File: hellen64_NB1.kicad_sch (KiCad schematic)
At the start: 170 parts, among them J1 USB_B_Mini, J11 Conn_01x01, J12 Conn_01x01, J13 Conn_01x01, J14 Conn_01x01, J15 Conn_01x01, J16 Conn_01x01, J17 Conn_01x01, J18 Conn_01x01, J19 Conn_01x01, J2 Conn_01x05_Male, J20 Conn_01x01, J21 Conn_01x01, J22 Conn_01x01, J24 Conn_01x01, J25 AudioJack3_SwitchTR, J27 Conn_01x06, J3 Conn_01x06, J4 Conn_02x12_Odd_Even, J5 USB_B, M1 Module-input-0.1, M10 Module-power12-0.2, M11 Module-power5-0.2, M12 Module-wbo-0.2, M13 Module-can-0.1, M2 Module-ign8-0.1, M3 Module-mcu-0.3, M4 Module-sd-0.1, M5 Module-output-0.2, M6 Module-dinput4-0.1, M7 Module-stlink-0.1, M8 Module-can-0.1, M9 Module-knock-0.1, P1 Pad, P10 Pad, P11 Pad, P12 Pad, P13 Pad, P14 Pad, P15 Pad, P17 Pad, P18 Pad, P19 Pad, P2 176122-6_2nd, P20 Pad, P22 Pad, P23 Pad, P24 Pad, P25 Pad, P26 Pad, P27 Pad, P28 Pad, P29 Pad, P3 Pad, P30 Pad, P31 Pad, P32 Pad, P34 Pad, P38 Pad, P4 Pad, P40 Pad, P43 Pad, P44 Pad, P46 Pad, P47 Pad, P48 Pad, P49 Pad, P5 Pad, P50 Pad, P51 Pad, P52 Pad, P53 Pad, P55 Pad, P56 Pad, P6 Pad, P7 Pad, P8 Pad, P9 Pad, U1 LIS2DW12TR, U2 MPX4_MAP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

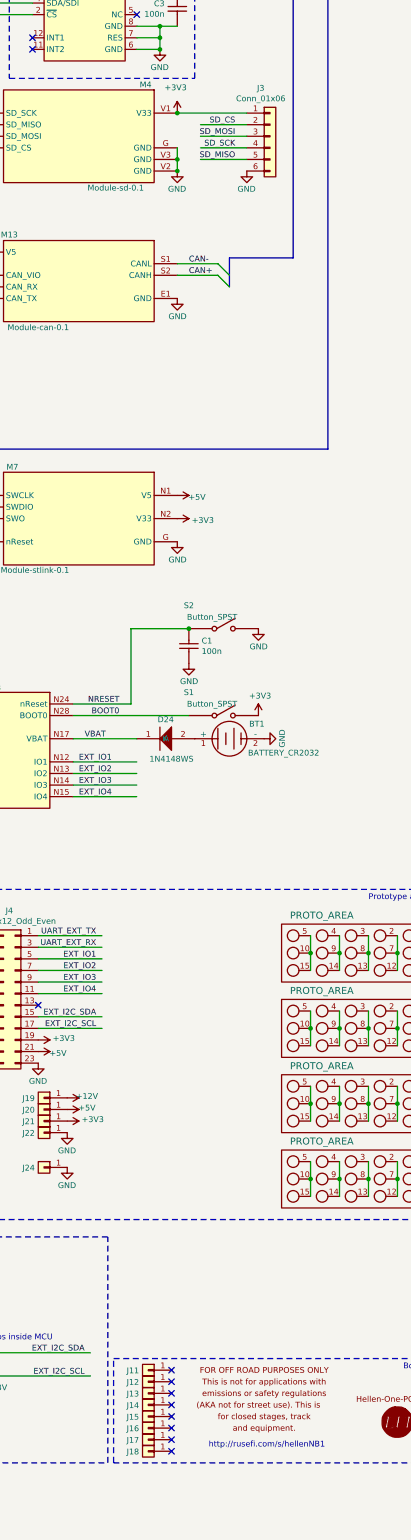
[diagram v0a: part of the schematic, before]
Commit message: new pcb board shape, dims & holes for NB1 + trying to fit components inside (remove SD-card ext.header)
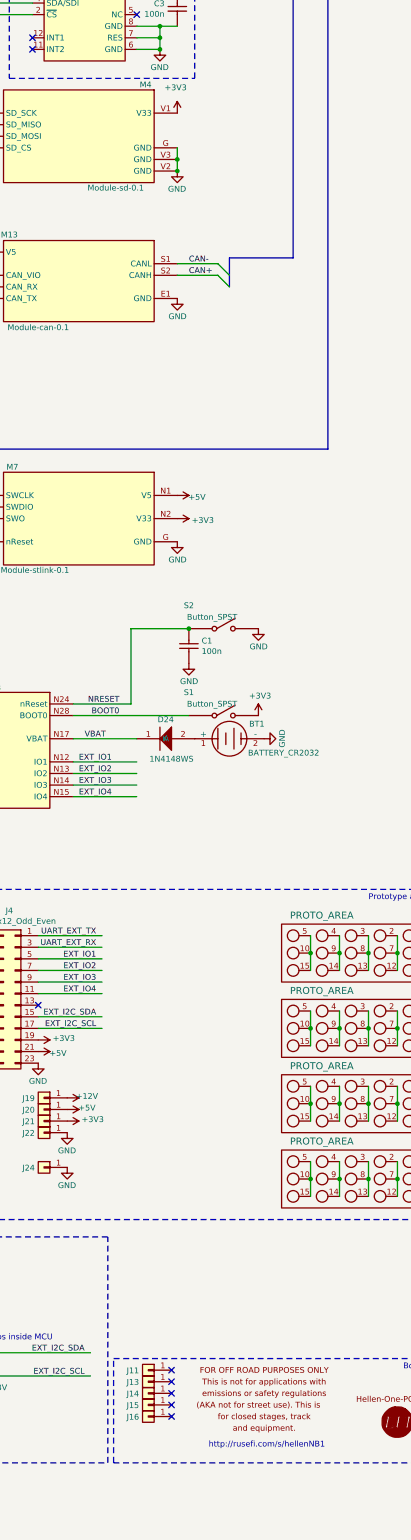
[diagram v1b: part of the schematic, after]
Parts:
- removed J12, J17, J18: Conn_01x01, MountingHole:MountingHole_4.5mm_Pad, symbol Connector_Generic:Conn_01x01
- removed J3: Conn_01x06, Connector_PinHeader_2.54mm:PinHeader_1x06_P2.54mm_Vertical, symbol Connector_Generic:Conn_01x06
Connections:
- no-connect marks 63 -> 60
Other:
- moved on the sheet: J13, J14, J15, J16
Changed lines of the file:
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@@
   (junction (at 515.62 74.93) (diameter 1.016) (color 0 0 0 0))
   (junction (at 515.62 77.47) (diameter 1.016) (color 0 0 0 0))
-  (junction (at 519.43 91.44) (diameter 1.016) (color 0 0 0 0))
   (junction (at 519.43 101.6) (diameter 1.016) (color 0 0 0 0))
   (junction (at 519.43 104.14) (diameter 1.016) (color 0 0 0 0))
@@
   (no_connect (at 518.16 374.65))
   (no_connect (at 518.16 377.19))
-  (no_connect (at 518.16 379.73))
-  (no_connect (at 518.16 382.27))
-  (no_connect (at 518.16 384.81))
   (bus_entry (at 77.47 27.94) (size 2.54 2.54)
     (stroke (width 0.1524) (type solid) (color 0 0 0 0))
@@
     (stroke (width 0) (type solid) (color 0 0 0 0))
   )
-  (wire (pts (xy 519.43 91.44) (xy 534.67 91.44))
-    (stroke (width 0) (type solid) (color 0 0 0 0))
-  )
   (wire (pts (xy 519.43 99.06) (xy 519.43 101.6))
     (stroke (width 0) (type solid) (color 0 0 0 0))
@@
     (stroke (width 0) (type solid) (color 0 0 0 0))
   )
-  (wire (pts (xy 524.51 93.98) (xy 534.67 93.98))
-    (stroke (width 0) (type solid) (color 0 0 0 0))
-  )
-  (wire (pts (xy 524.51 96.52) (xy 534.67 96.52))
-    (stroke (width 0) (type solid) (color 0 0 0 0))
-  )
-  (wire (pts (xy 524.51 99.06) (xy 534.67 99.06))
-    (stroke (width 0) (type solid) (color 0 0 0 0))
-  )
-  (wire (pts (xy 524.51 101.6) (xy 534.67 101.6))
-    (stroke (width 0) (type solid) (color 0 0 0 0))
-  )
   (wire (pts (xy 548.64 271.78) (xy 548.64 275.59))
     (stroke (width 0) (type solid) (color 0 0 0 0))
@@
     (effects (font (size 1.27 1.27)) (justify left bottom))
   )
-  (label "SD_CS" (at 532.13 93.98 180)
-    (effects (font (size 1.27 1.27)) (justify right bottom))
-  )
-  (label "SD_MOSI" (at 532.13 96.52 180)
-    (effects (font (size 1.27 1.27)) (justify right bottom))
-  )
-  (label "SD_SCK" (at 532.13 99.06 180)
-    (effects (font (size 1.27 1.27)) (justify right bottom))
-  )
-  (label "SD_MISO" (at 532.13 101.6 180)
-    (effects (font (size 1.27 1.27)) (justify right bottom))
-  )
   (symbol (lib_id "power:+5V") (at 31.75 318.77 90) (unit 1)
     (in_bom yes) (on_board yes)
@@
     (pin "1")
   )
-  (symbol (lib_id "power:GND") (at 534.67 104.14 0) (mirror y) (unit 1)
-    (in_bom yes) (on_board yes)
-    (property "Reference" "#PWR0103" (id 0) (at 534.67 110.49 0)
-      (effects (font (size 1.27 1.27)) hide)
-    )
-    (property "Value" "GND" (id 1) (at 534.6192 108.0834 0))
-    (property "Footprint" "" (id 2) (at 534.67 104.14 0)
-      (effects (font (size 1.27 1.27)) hide)
-    )
-    (property "Datasheet" "" (id 3) (at 534.67 104.14 0)
-      (effects (font (size 1.27 1.27)) hide)
-    )
-    (pin "1")
-  )
   (symbol (lib_id "power:GND") (at 537.21 204.47 0) (unit 1)
     (in_bom yes) (on_board yes)
@@
   (symbol (lib_id "Connector_Generic:Conn_01x01") (at 513.08 369.57 0) (mirror y) (unit 1)
     (in_bom yes) (on_board yes)
-    (property "Reference" "J12" (id 0) (at 511.048 369.6716 0)
+    (property "Reference" "J13" (id 0) (at 511.048 369.6716 0)
       (effects (font (size 1.27 1.27)) (justify left))
     )
@@
   (symbol (lib_id "Connector_Generic:Conn_01x01") (at 513.08 372.11 0) (mirror y) (unit 1)
     (in_bom yes) (on_board yes)
-    (property "Reference" "J13" (id 0) (at 511.048 372.2116 0)
+    (property "Reference" "J14" (id 0) (at 511.048 372.2116 0)
       (effects (font (size 1.27 1.27)) (justify left))
     )
@@
   (symbol (lib_id "Connector_Generic:Conn_01x01") (at 513.08 374.65 0) (mirror y) (unit 1)
     (in_bom yes) (on_board yes)
-    (property "Reference" "J14" (id 0) (at 511.048 374.7516 0)
+    (property "Reference" "J15" (id 0) (at 511.048 374.7516 0)
       (effects (font (size 1.27 1.27)) (justify left))
     )
@@
   (symbol (lib_id "Connector_Generic:Conn_01x01") (at 513.08 377.19 0) (mirror y) (unit 1)
     (in_bom yes) (on_board yes)
-    (property "Reference" "J15" (id 0) (at 511.048 377.2916 0)
+    (property "Reference" "J16" (id 0) (at 511.048 377.2916 0)
       (effects (font (size 1.27 1.27)) (justify left))
     )
@@
     (pin "1")
   )
-  (symbol (lib_id "Connector_Generic:Conn_01x01") (at 513.08 379.73 0) (mirror y) (unit 1)
-    (in_bom yes) (on_board yes)
-    (property "Reference" "J16" (id 0) (at 511.048 379.8316 0)
-      (effects (font (size 1.27 1.27)) (justify left))
-    )
-    (property "Value" "Conn_01x01" (id 1) (at 511.048 380.9746 0)
-      (effects (font (size 1.27 1.27)) (justify left) hide)
-    )
-    (property "Footprint" "MountingHole:MountingHole_4.5mm_Pad" (id 2) (at 513.08 379.73 0)
-      (effects (font (size 1.27 1.27)) hide)
-    )
-    (property "Datasheet" "~" (id 3) (at 513.08 379.73 0)
-      (effects (font (size 1.27 1.27)) hide)
-    )
-    (pin "1")
-  )
-  (symbol (lib_id "Connector_Generic:Conn_01x01") (at 513.08 382.27 0) (mirror y) (unit 1)
-    (in_bom yes) (on_board yes)
-    (property "Reference" "J17" (id 0) (at 511.048 382.3716 0)
-      (effects (font (size 1.27 1.27)) (justify left))
-    )
-    (property "Value" "Conn_01x01" (id 1) (at 511.048 383.5146 0)
-      (effects (font (size 1.27 1.27)) (justify left) hide)
-    )
-    (property "Footprint" "MountingHole:MountingHole_4.5mm_Pad" (id 2) (at 513.08 382.27 0)
-      (effects (font (size 1.27 1.27)) hide)
-    )
-    (property "Datasheet" "~" (id 3) (at 513.08 382.27 0)
-      (effects (font (size 1.27 1.27)) hide)
-    )
-    (pin "1")
-  )
-  (symbol (lib_id "Connector_Generic:Conn_01x01") (at 513.08 384.81 0) (mirror y) (unit 1)
-    (in_bom yes) (on_board yes)
-    (property "Reference" "J18" (id 0) (at 511.048 384.9116 0)
-      (effects (font (size 1.27 1.27)) (justify left))
-    )
-    (property "Value" "Conn_01x01" (id 1) (at 511.048 386.0546 0)
-      (effects (font (size 1.27 1.27)) (justify left) hide)
-    )
-    (property "Footprint" "MountingHole:MountingHole_4.5mm_Pad" (id 2) (at 513.08 384.81 0)
-      (effects (font (size 1.27 1.27)) hide)
-    )
-    (property "Datasheet" "~" (id 3) (at 513.08 384.81 0)
-      (effects (font (size 1.27 1.27)) hide)
-    )
-    (pin "1")
-  )
   (symbol (lib_id "hellen-one-common:Res") (at 90.17 313.69 0) (mirror y) (unit 1)
     (in_bom yes) (on_board yes)
@@
     (pin "6")
   )
-  (symbol (lib_id "Connector_Generic:Conn_01x06") (at 539.75 96.52 0) (unit 1)
-    (in_bom yes) (on_board yes)
-    (property "Reference" "J3" (id 0) (at 537.718 85.9598 0))
-    (property "Value" "Conn_01x06" (id 1) (at 537.718 88.2585 0))
-    (property "Footprint" "Connector_PinHeader_2.54mm:PinHeader_1x06_P2.54mm_Vertical" (id 2) (at 539.75 96.52 0)
-      (effects (font (size 1.27 1.27)) hide)
-    )
-    (property "Datasheet" "~" (id 3) (at 539.75 96.52 0)
-      (effects (font (size 1.27 1.27)) hide)
-    )
-    (pin "1")
-    (pin "2")
-    (pin "3")
-    (pin "4")
-    (pin "5")
-    (pin "6")
-  )
   (symbol (lib_id "hellen-one-common:LED_0603") (at 53.34 384.81 0) (mirror y) (unit 1)
     (in_bom yes) (on_board yes)
@@
       (reference "#PWR0102") (unit 1) (value "+5VA") (footprint "")
     )
-    (path "/92887baa-5735-435e-849f-a23e5b2533af"
-      (reference "#PWR0103") (unit 1) (value "GND") (footprint "")
-    )
     (path "/5fe6fb57-f54b-4b13-b913-34e51ba31b59"
       (reference "#PWR0104") (unit 1) (value "GND") (footprint "")
@@
       (reference "J2") (unit 1) (value "Conn_01x05_Male") (footprint "Connector_Molex:Molex_SPOX_5267-05A_1x05_P2.50mm_Vertical")
     )
-    (path "/6aa321a6-af89-4106-8dab-5049a056c4bb"
-      (reference "J3") (unit 1) (value "Conn_01x06") (footprint "Connector_PinHeader_2.54mm:PinHeader_1x06_P2.54mm_Vertical")
-    )
     (path "/a73c9bfe-6b19-47cd-8a47-b0140dfc9eca"
       (reference "J4") (unit 1) (value "Conn_02x12_Odd_Even") (footprint "Connector_PinHeader_2.54mm:PinHeader_2x12_P2.54mm_Vertical")
@@
       (reference "J11") (unit 1) (value "Conn_01x01") (footprint "MountingHole:MountingHole_4.5mm_Pad")
     )
-    (path "/b6b17510-f2fd-4be9-af2b-0ed340671ca7"
-      (reference "J12") (unit 1) (value "Conn_01x01") (footprint "MountingHole:MountingHole_4.5mm_Pad")
-    )
     (path "/ffccce6a-be03-48d4-af6d-019854539260"
       (reference "J13") (unit 1) (value "Conn_01x01") (footprint "MountingHole:MountingHole_4.5mm_Pad")
@@
       (reference "J16") (unit 1) (value "Conn_01x01") (footprint "MountingHole:MountingHole_4.5mm_Pad")
     )
-    (path "/b071a9f3-95cd-4732-82c7-2d419ca96271"
-      (reference "J17") (unit 1) (value "Conn_01x01") (footprint "MountingHole:MountingHole_4.5mm_Pad")
-    )
-    (path "/297cb064-b85c-4512-9bd4-e6a9315f74ca"
-      (reference "J18") (unit 1) (value "Conn_01x01") (footprint "MountingHole:MountingHole_4.5mm_Pad")
-    )
     (path "/8c69e9f7-b55c-4581-a735-a2fe0d5311f2"

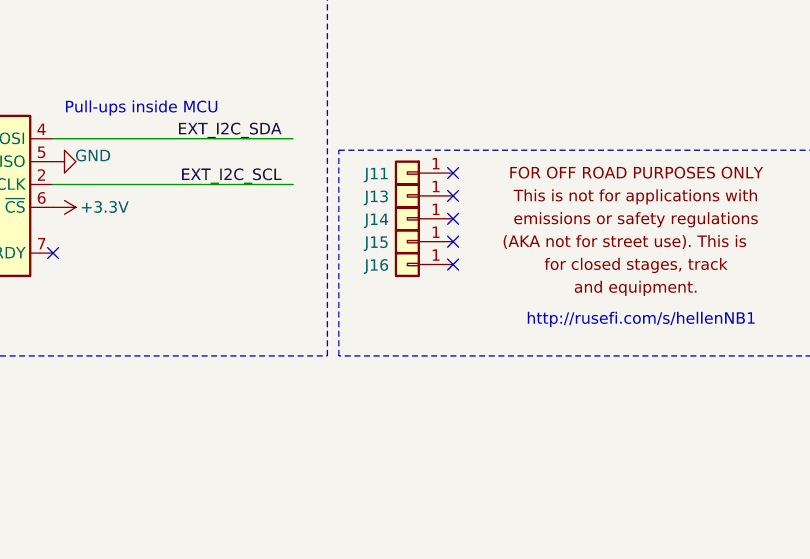
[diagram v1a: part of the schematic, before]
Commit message: New 178780-1 76p connector footprint & board holes
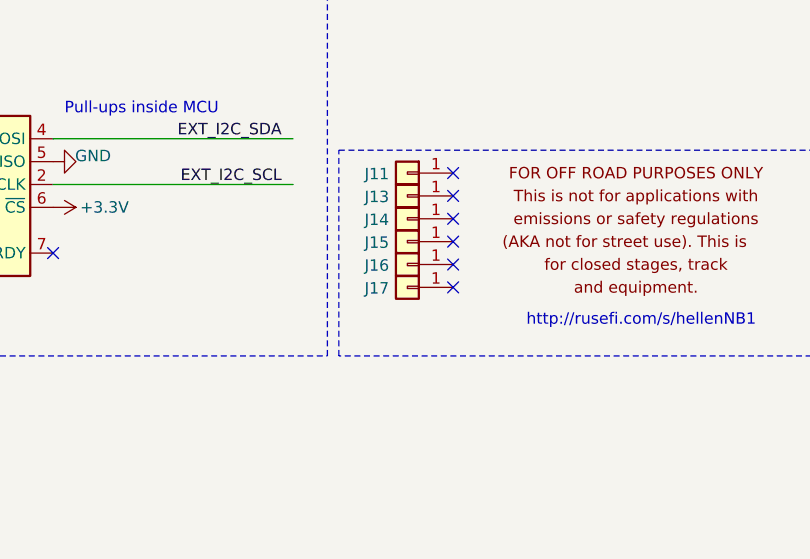
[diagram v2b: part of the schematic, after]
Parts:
- added J17: Conn_01x01, MountingHole:MountingHole_4.5mm_Pad, symbol Connector_Generic:Conn_01x01
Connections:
- no-connect marks 60 -> 61
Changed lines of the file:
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@@
   (no_connect (at 518.16 374.65))
   (no_connect (at 518.16 377.19))
+  (no_connect (at 518.16 379.73))
   (bus_entry (at 77.47 27.94) (size 2.54 2.54)
     (stroke (width 0.1524) (type solid) (color 0 0 0 0))
@@
     (pin "1")
   )
+  (symbol (lib_id "Connector_Generic:Conn_01x01") (at 513.08 379.73 0) (mirror y) (unit 1)
+    (in_bom yes) (on_board yes)
+    (property "Reference" "J17" (id 0) (at 511.048 379.8316 0)
+      (effects (font (size 1.27 1.27)) (justify left))
+    )
+    (property "Value" "Conn_01x01" (id 1) (at 511.048 380.9746 0)
+      (effects (font (size 1.27 1.27)) (justify left) hide)
+    )
+    (property "Footprint" "MountingHole:MountingHole_4.5mm_Pad" (id 2) (at 513.08 379.73 0)
+      (effects (font (size 1.27 1.27)) hide)
+    )
+    (property "Datasheet" "~" (id 3) (at 513.08 379.73 0)
+      (effects (font (size 1.27 1.27)) hide)
+    )
+    (pin "1")
+  )
   (symbol (lib_id "hellen-one-common:Res") (at 90.17 313.69 0) (mirror y) (unit 1)
     (in_bom yes) (on_board yes)
@@
       (reference "J16") (unit 1) (value "Conn_01x01") (footprint "MountingHole:MountingHole_4.5mm_Pad")
     )
+    (path "/1c6ff2af-f264-4fc0-8826-fea36c657dd4"
+      (reference "J17") (unit 1) (value "Conn_01x01") (footprint "MountingHole:MountingHole_4.5mm_Pad")
+    )
     (path "/8c69e9f7-b55c-4581-a735-a2fe0d5311f2"

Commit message: update schematic
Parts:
- removed P26, P40: Pad, hellen-one-common:PAD-TH, symbol hellen-one-common:Pad
- added D32: 1N4148WS, hellen-one-common:SOD-323, symbol hellen-one-common:1N4148WS
- added F2: Fuse-Pad-Pad, hellen-one-common:PAD-1206-PAD, symbol hellen-one-common:Fuse-Pad-Pad
- added unit 4 of P2
- added R8: Jumper-Pad-Pad, hellen-one-common:PAD-0805-PAD, symbol hellen-one-common:Jumper-Pad-Pad
- P2: value 176122-6_2nd -> 178780-1; footprint rusefi_lib:176122-6_2nd -> hellen-one-common:178780-1; symbol 176122-6:176122-6_2nd -> hellen-one-common:178780-1
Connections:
- net D2 is gone; now on net CLUTCH: M3.S4 (IN_D2), M6.W3 (OUT_D2)
- net IN_D2 is gone; now on net IN_CLUTCH: M6.V3 (IN_D2)
- net +12V_PROT: now also D32.1 (K)
- net +5VA: now also P2.73 (4F)
- net 1B: now also F2.2
- net 3T: now also R8.2; no longer R43.2
- net CLUTCH: no longer M1.N9 (AUX2), M3.S25 (IN_AUX2)
- net GND: now also P2.65 (4A)
- net IN_CLUTCH: no longer M1.S18 (IN_AUX2)
- net OUT_AC_FAN_RELAY: now also M5.W1 (OUT_LOW2); no longer M5.W10 (OUT_INJ5)
- net WBO_Ip: now also P2.75 (4J)
- net WBO_R_Trim: now also P2.69 (4I)
- net WBO_Vs: now also P2.74 (4H)
- net WBO_Vs/Ip: now also P2.68 (4G)
- net AUX1 renamed PRESSURE
- net AUX4 renamed EGR_BOOST
- net D1 renamed DIGITAL
- net IN_D1 renamed IN_DIGITAL
- net IN_DIGITAL: now also P2.71 (4B)
- net O2S2 renamed AFR
- net OUT_EGR_BOOST renamed OUT_BOOST
- net OUT_BOOST: now also R8.1
- net RES1 renamed BRAKE
- net RES2 renamed STEERING
- net SENS4 renamed NEUTRAL
- net WBO_H- renamed 4K
- net 4K: now also P2.70 (4K)
- new net: P2.72 (4D), R43.2
- new net 4L: F2.1, P2.76 (4L)
- new net IN_TEMP: M1.S18 (IN_AUX2), P2.66 (4C)
- new net OUT_VVT: D32.2 (A), M5.W10 (OUT_INJ5), P2.67 (4E)
- new net TEMP: M1.N9 (AUX2), M3.S25 (IN_AUX2)
- no-connect marks 61 -> 55
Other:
- note added: "WBO_H+"
- moved on the sheet: C2, M9, P1, R43, U2

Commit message: update schematics - ETB
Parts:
- removed P27: Pad, hellen-one-common:PAD-TH, symbol hellen-one-common:Pad
- added C10: 10nF, Capacitor_SMD:C_0402_1005Metric, symbol Device:C
- added C11, C12, C13, C15, C17, C19, C7, C9: 10uF, Capacitor_SMD:C_0603_1608Metric, symbol Device:C
- added C14: 220nF, Capacitor_SMD:C_0402_1005Metric, symbol Device:C
- added C16, C18: 100nF, Capacitor_SMD:C_0402_1005Metric, symbol Device:C
- added C8: 5.6nF, Capacitor_SMD:C_0402_1005Metric, symbol Device:C
- added D33, D34: 1N4148WS, Diode_SMD:D_SOD-323, symbol Device:D
- added J3: MiniFit, Connector_Molex:Molex_Mini-Fit_Jr_5569-02A2_2x01_P4.20mm_Horizontal, symbol Connector_Generic:Conn_01x02
- added J6: ETB, Connector_PinHeader_2.54mm:PinHeader_1x06_P2.54mm_Vertical, symbol Connector_Generic:Conn_01x06
- added R10: 100, Resistor_SMD:R_0402_1005Metric, symbol Device:R
- added R19: 10k, Resistor_SMD:R_0402_1005Metric, symbol Device:R
- added R21: Jumper-Pad-Pad, hellen-one-common:PAD-0805-PAD, symbol hellen-one-common:Jumper-Pad-Pad
- added R9: 100k, Resistor_SMD:R_0402_1005Metric, symbol Device:R
- added U5: L6205PD, kicad6:SO20POWER, symbol L6205PD:L6205PD
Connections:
- net IN_D3 is gone; now on net IN_NEUTRAL: M6.V4 (IN_D3)
- net +5V: now also M6.J2 (PULL_D2), M6.J3 (PULL_D3)
- net +5VA: now also J6.1 (Pin_1)
- net GND: now also C11.2, C12.2, C13.2, C15.2, C16.2, C17.2, C18.2, C19.2, C7.2, C8.2, C9.2, J6.6 (Pin_6), R19.1, U5.1 (GND@1), U5.10 (GND@2), U5.11 (GND@3), U5.13 (SENSEB), U5.20 (GND@4), U5.8 (SENSEA), U5.SLUG1 (SLUG@1), U5.SLUG2 (SLUG@2), U5.SLUG3 (SLUG@3); no longer M6.J2 (PULL_D2), M6.J3 (PULL_D3)
- net IN_NEUTRAL: no longer M1.S4 (IN_SENS4)
- net IN_PPS: now also J6.4 (Pin_4)
- net IN_TEMP: no longer P2.66 (4C)
- net IN_TPS: now also J6.2 (Pin_2)
- net SOLENOID_A1 renamed ETB_EN
- net ETB_EN: now also R19.2, R9.2
- net SOLENOID_A2 renamed +ETB
- net +ETB: now also U5.15 (IN2B), U5.7 (IN2A)
- net SOLENOID_B1 renamed -ETB
- net -ETB: now also U5.14 (IN1B), U5.6 (IN1A)
- new net: C10.1, R10.1
- new net: D33.1 (K), D34.2 (A), R10.2
- new net: C14.2, D34.1 (K), U5.17 (VBOOT)
- new net: P2.66 (4C), R21.2
- new net: C8.1, R9.1, U5.16 (ENB), U5.5 (ENA)
- new net: C10.2, U5.4 (VCP)
- new net IN_TEMP_OR_PPS2: R21.1
- new net IN_TPS2: J6.3 (Pin_3), M1.S4 (IN_SENS4)
- new net OUT_ETB+: J3.2 (Pin_2), U5.18 (OUT2B), U5.3 (OUT2A)
- new net OUT_ETB-: J3.1 (Pin_1), U5.12 (OUT1B), U5.9 (OUT1A)
- new net V12_RAW: C11.1, C12.1, C13.1, C14.1, C15.1, C16.1, C17.1, C18.1, C19.1, C7.1, C9.1, D33.2 (A), U5.19 (VSB), U5.2 (VSA)
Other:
- note added: "ETB driver"
- moved on the sheet: C5, D1, D10, D11, D12, D13, D14, D15, D16, D17, D18, D19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

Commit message: update
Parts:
- removed C7: 10uF, Capacitor_SMD:C_0603_1608Metric, symbol Device:C
- removed P46: Pad, hellen-one-common:PAD-TH, symbol hellen-one-common:Pad
- added C18, C20: 10uF, hellen-one-common:C0805, symbol Device:C
- added F3: Fuse-Pad-Pad, hellen-one-common:PAD-1206-PAD, symbol hellen-one-common:Fuse-Pad-Pad
- added R22: Jumper-Pad-Pad, hellen-one-common:PAD-0805-PAD, symbol hellen-one-common:Jumper-Pad-Pad
- C10: footprint Capacitor_SMD:C_0402_1005Metric -> hellen-one-common:C0603; LCSC C541443 -> C57112
- C11, C12, C13, C15, C17, C19, C9: footprint Capacitor_SMD:C_0603_1608Metric -> hellen-one-common:C0805; LCSC C87152 -> C15850
- C14: footprint Capacitor_SMD:C_0402_1005Metric -> hellen-one-common:C0603; LCSC C106258 -> C21120
- C16: value 100nF -> 10uF; footprint Capacitor_SMD:C_0402_1005Metric -> hellen-one-common:C0805; LCSC C105882 -> C15850
- C7: renamed from C18; footprint Capacitor_SMD:C_0402_1005Metric -> hellen-one-common:C0603; LCSC C105882 -> C14663
- C8: value 5.6nF -> 6.8nF; footprint Capacitor_SMD:C_0402_1005Metric -> hellen-one-common:C0603; LCSC C115688 -> C1631
- D33, D34: footprint Diode_SMD:D_SOD-323 -> hellen-one-common:SOD-323
- J3: footprint Connector_Molex:Molex_Mini-Fit_Jr_5569-02A2_2x01_P4.20mm_Horizontal -> hellen-one-common:Molex-39301020; LCSC (none) -> C240832
- J6: footprint Connector_PinHeader_2.54mm:PinHeader_1x06_P2.54mm_Vertical -> hellen-one-common:PinHeader_1x06_P2.54mm_Vertical
- P2: symbol hellen-one-common:178780-1 -> 178780-1:178780-1
- R10: footprint Resistor_SMD:R_0402_1005Metric -> hellen-one-common:R0603; LCSC C106233 -> C22775
- R19: footprint Resistor_SMD:R_0402_1005Metric -> hellen-one-common:R0603; LCSC C60489 -> C25804
- R9: footprint Resistor_SMD:R_0402_1005Metric -> hellen-one-common:R0603; LCSC C106234 -> C25803
- U5: footprint kicad6:SO20POWER -> hellen-one-common:SO20POWER
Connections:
- net 1B: now also F3.1
- net 1Q: now also R22.2
- net GND: now also C16.1, C19.1, C7.1, C18.2, C20.1; no longer C16.2, C19.2, C7.2
- net IN_TEMP_OR_PPS2: now also J6.5 (Pin_5)
- net OUT_ALT_WARNING: now reaches M5.S13 (OUT_LOW12)
- net OUT_ALT_WARNING: now also R22.1
- net LOW11 renamed ALT_WARN
- net V12_RAW renamed +12V_ETB
- net +12V_ETB: now also C16.2, C19.2, C7.2, C18.1, C20.2, F3.2; no longer C16.1, C19.1, C7.1
- no-connect marks 55 -> 54
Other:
- moved on the sheet: C7, J6
